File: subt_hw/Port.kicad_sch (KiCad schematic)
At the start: 4 parts, among them J100 RJ45, U100 MAX487E

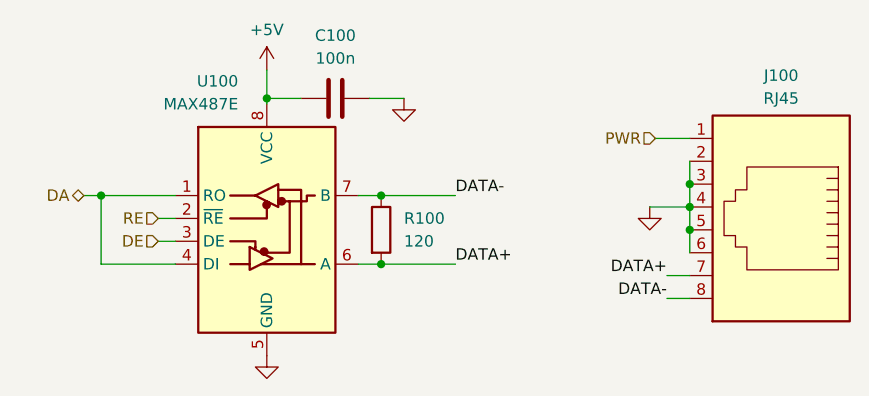
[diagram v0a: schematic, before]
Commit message: Simplify wiring
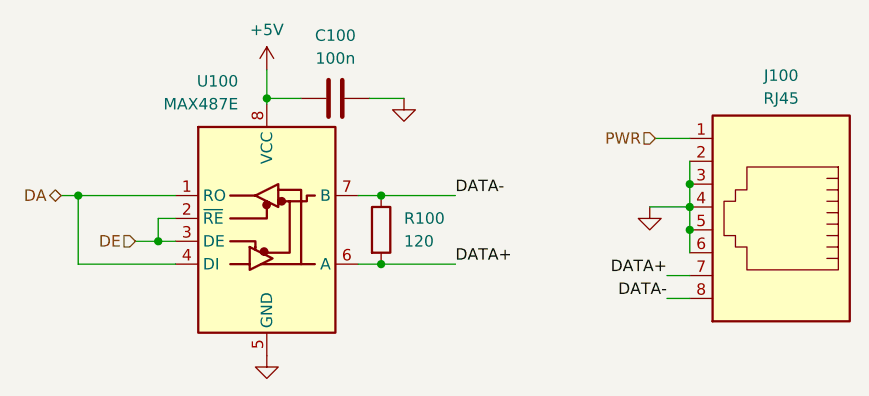
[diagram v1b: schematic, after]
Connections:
- net RE is gone; now on net DE: U100.2 (~{RE})
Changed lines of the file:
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@@
 (kicad_sch (version 20230121) (generator eeschema)
   (paper "A4")
-  (junction (at 27.305 45.085) (diameter 0) (color 0 0 0 0)
+  (junction (at 24.765 45.085) (diameter 0) (color 0 0 0 0)
   )
   (junction (at 45.72 34.29) (diameter 0) (color 0 0 0 0)
   )
   (junction (at 58.42 52.705) (diameter 0) (color 0 0 0 0)
+  )
+  (junction (at 33.655 50.165) (diameter 0) (color 0 0 0 0)
   )
   (junction (at 92.71 46.355) (diameter 0) (color 0 0 0 0)
@@
   (junction (at 92.71 43.815) (diameter 0) (color 0 0 0 0)
   )
-  (wire (pts (xy 33.655 50.165) (xy 35.56 50.165))
+  (wire (pts (xy 31.115 50.165) (xy 33.655 50.165))
     (stroke (width 0) (type default))
   )
@@
     (stroke (width 0) (type default))
   )
-  (wire (pts (xy 25.4 45.085) (xy 27.305 45.085))
+  (wire (pts (xy 22.86 45.085) (xy 24.765 45.085))
+    (stroke (width 0) (type default))
+  )
+  (wire (pts (xy 33.655 50.165) (xy 35.56 50.165))
     (stroke (width 0) (type default))
   )
@@
     (stroke (width 0) (type default))
   )
-  (wire (pts (xy 27.305 45.085) (xy 35.56 45.085))
+  (wire (pts (xy 24.765 45.085) (xy 35.56 45.085))
     (stroke (width 0) (type default))
   )
@@
     (stroke (width 0) (type default))
   )
-  (wire (pts (xy 27.305 52.705) (xy 35.56 52.705))
+  (wire (pts (xy 24.765 52.705) (xy 35.56 52.705))
+    (stroke (width 0) (type default))
+  )
+  (wire (pts (xy 33.655 47.625) (xy 33.655 50.165))
     (stroke (width 0) (type default))
   )
@@
     (stroke (width 0) (type default))
   )
-  (wire (pts (xy 27.305 52.705) (xy 27.305 45.085))
+  (wire (pts (xy 24.765 52.705) (xy 24.765 45.085))
     (stroke (width 0) (type default))
   )
@@
     (effects (font (size 1.27 1.27)) (justify right bottom))
   )
-  (hierarchical_label "RE" (shape input) (at 33.655 47.625 180) (fields_autoplaced)
-    (effects (font (size 1.27 1.27)) (justify right))
-  )
-  (hierarchical_label "DE" (shape input) (at 33.655 50.165 180) (fields_autoplaced)
+  (hierarchical_label "DE" (shape input) (at 31.115 50.165 180) (fields_autoplaced)
     (effects (font (size 1.27 1.27)) (justify right))
   )
@@
     (effects (font (size 1.27 1.27)) (justify right))
   )
-  (hierarchical_label "DA" (shape bidirectional) (at 25.4 45.085 180) (fields_autoplaced)
+  (hierarchical_label "DA" (shape bidirectional) (at 22.86 45.085 180) (fields_autoplaced)
     (effects (font (size 1.27 1.27)) (justify right))
   )
